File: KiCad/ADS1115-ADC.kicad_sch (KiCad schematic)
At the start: 19 parts, among them J1 Conn_01x05_Pin, U1 LM334M, U2 LM334M, U3 ADS1115IDGS

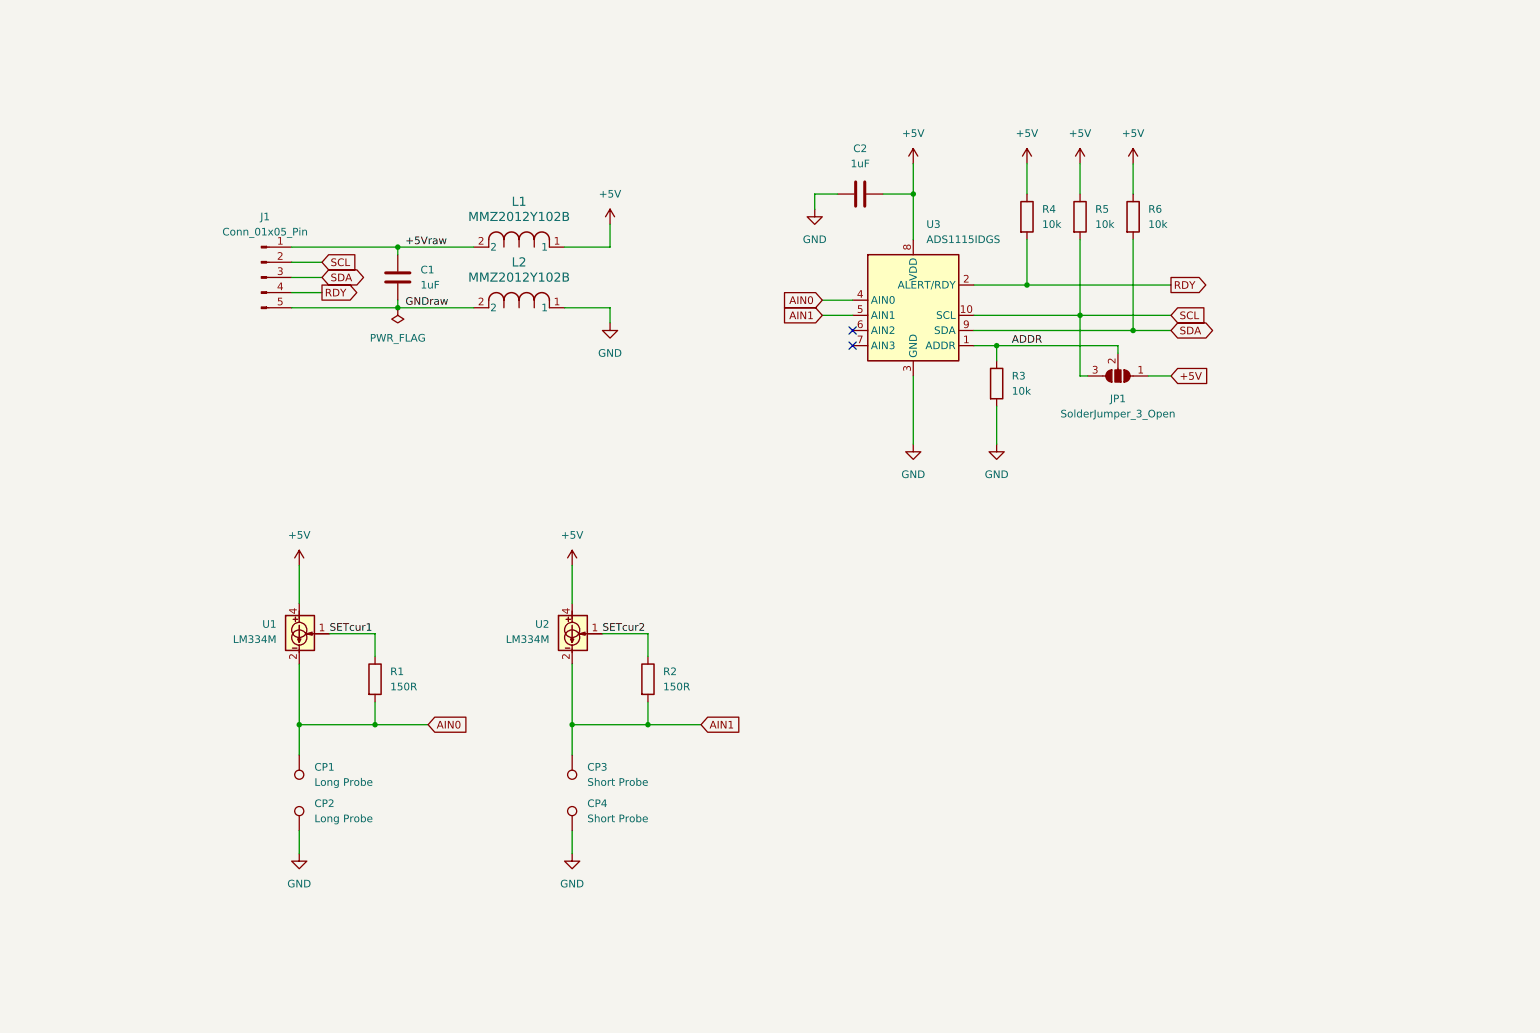
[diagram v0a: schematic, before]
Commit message: Add level shifters
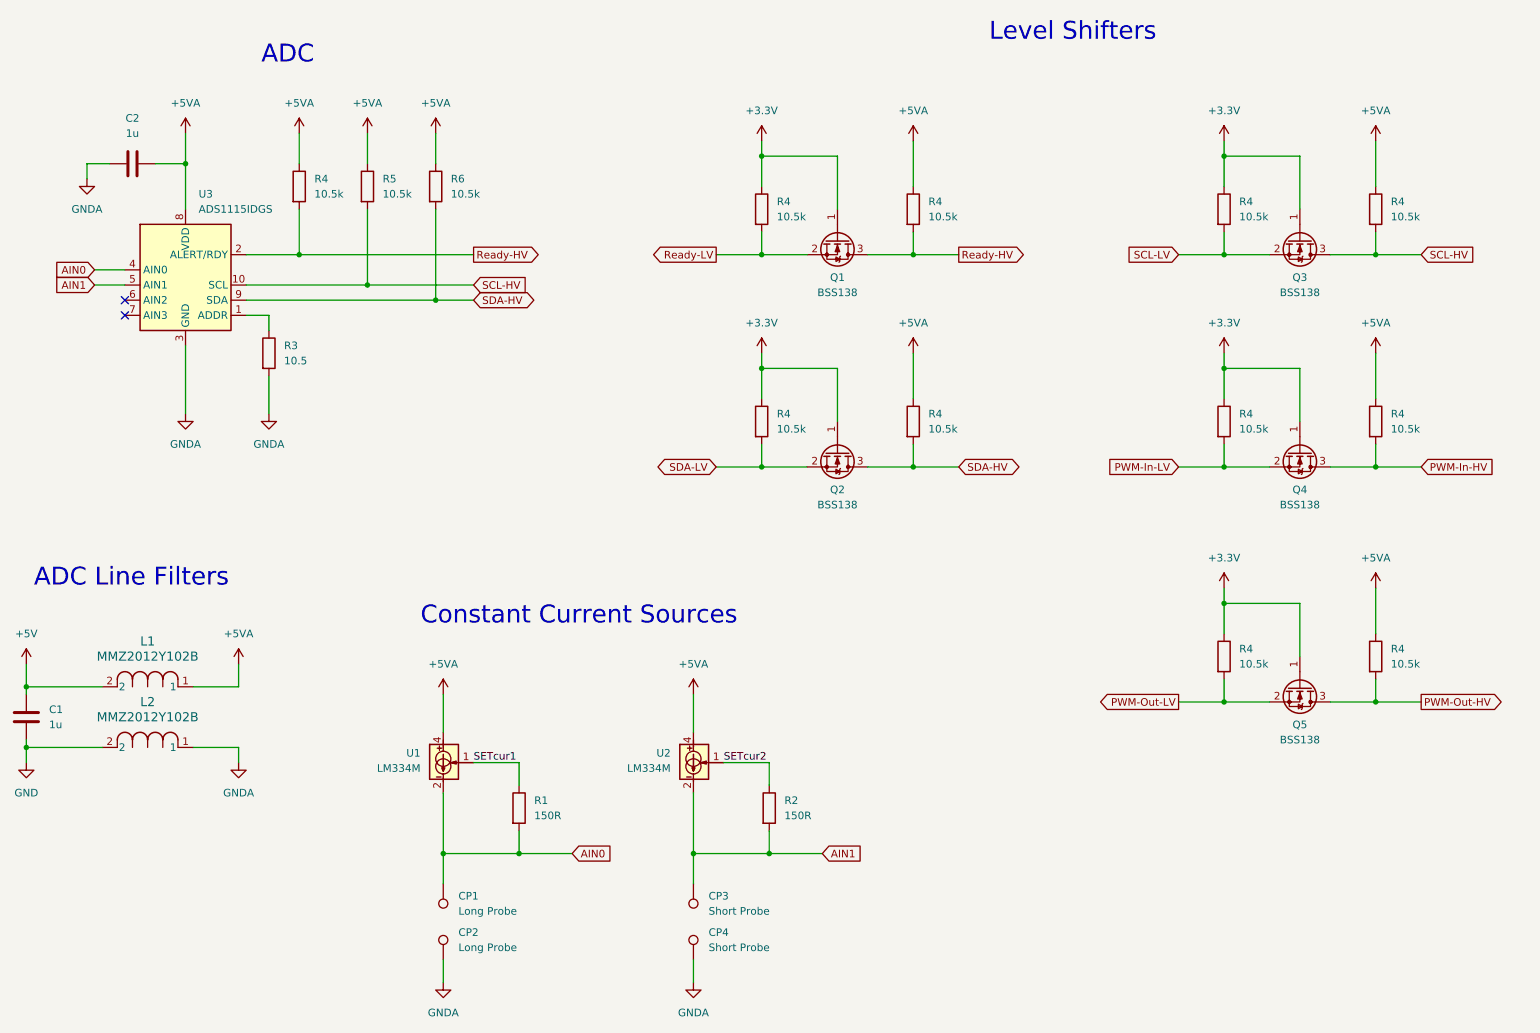
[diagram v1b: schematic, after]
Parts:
- removed J1: Conn_01x05_Pin, Connector_PinHeader_2.54mm:PinHeader_1x05_P2.54mm_Horizontal, symbol Connector:Conn_01x05_Pin
- removed JP1: SolderJumper_3_Open, Jumper:SolderJumper-3_P1.3mm_Open_RoundedPad1.0x1.5mm, symbol Jumper:SolderJumper_3_Open
- added Q1, Q2, Q3, Q4, Q5: BSS138, Package_TO_SOT_SMD:SOT-23, symbol Transistor_FET:BSS138
- added R4 (x10): 10.5k, Resistor_SMD:R_0402_1005Metric_Pad0.72x0.64mm_HandSolder, symbol Device:R
- C1, C2: value 1uF -> 1u; footprint Capacitor_SMD:C_1206_3216Metric_Pad1.33x1.80mm_HandSolder -> Capacitor_SMD:C_0402_1005Metric_Pad0.74x0.62mm_HandSolder
- R1, R2: footprint Resistor_SMD:R_1206_3216Metric_Pad1.30x1.75mm_HandSolder -> Resistor_SMD:R_0402_1005Metric_Pad0.72x0.64mm_HandSolder
- R3: value 10k -> 10.5; footprint Resistor_SMD:R_1206_3216Metric_Pad1.30x1.75mm_HandSolder -> Resistor_SMD:R_0402_1005Metric_Pad0.72x0.64mm_HandSolder
- R4, R5, R6: value 10k -> 10.5k; footprint Resistor_SMD:R_1206_3216Metric_Pad1.30x1.75mm_HandSolder -> Resistor_SMD:R_0402_1005Metric_Pad0.72x0.64mm_HandSolder
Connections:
- net +5Vraw is gone; now on net +5V: C1.1, L1.2
- net GNDraw is gone; now on net GND: C1.2, L2.2
- net +5V: no longer C2.2, L1.1, R4.1, R5.1, R6.1, U1.4, U2.4, U3.8 (VDD)
- net GND: no longer C2.1, CP2.1, CP4.1, L2.1, R3.2, U3.3 (GND)
- net ADDR: no longer names the net of R3.1, U3.1 (ADDR)
- net RDY renamed Ready-HV
- net Ready-HV: now also Q1.3 (D), R4.2
- net SCL renamed SCL-HV
- net SCL-HV: now also Q3.3 (D), R4.2
- net SDA renamed SDA-HV
- net SDA-HV: now also Q2.3 (D), R4.2
- new net +3.3V: Q1.1 (G), Q2.1 (G), Q3.1 (G), Q4.1 (G), Q5.1 (G), R4.1, R4.1, R4.1, R4.1, R4.1
- new net +5VA: C2.2, L1.1, R4.1, R4.1, R4.1, R4.1, R4.1, R4.1, R5.1, R6.1, U1.4, U2.4, U3.8 (VDD)
- new net GNDA: C2.1, CP2.1, CP4.1, L2.1, R3.2, U3.3 (GND)
- new net PWM-In-HV: Q4.3 (D), R4.2
- new net PWM-In-LV: Q4.2 (S), R4.2
- new net PWM-Out-HV: Q5.3 (D), R4.2
- new net PWM-Out-LV: Q5.2 (S), R4.2
- new net Ready-LV: Q1.2 (S), R4.2
- new net SCL-LV: Q3.2 (S), R4.2
- new net SDA-LV: Q2.2 (S), R4.2
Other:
- note added: "ADC"
- note added: "ADC Line Filters"
- note added: "Constant Current Sources"
- note added: "Level Shifters"
- moved on the sheet: C1, C2, CP1, CP2, CP3, CP4, L1, L2, R1, R2, R3, R4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

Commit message: Change resistor values
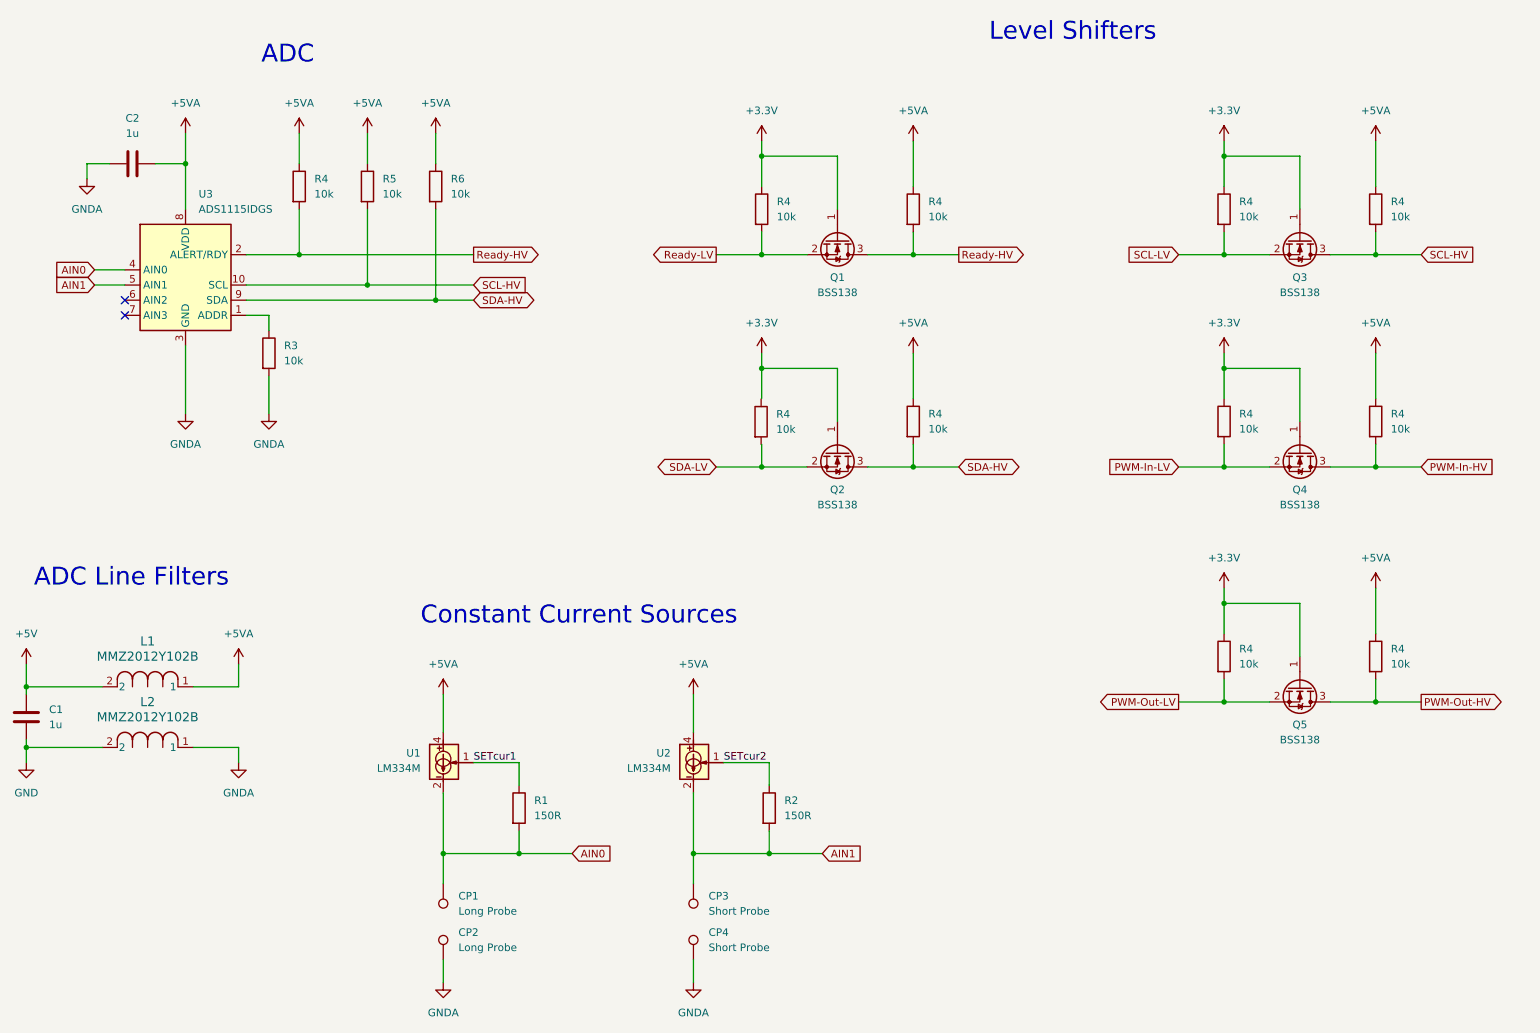
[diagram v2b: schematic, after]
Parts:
- removed R4 (x9): 10.5k, Resistor_SMD:R_0402_1005Metric_Pad0.72x0.64mm_HandSolder, symbol Device:R
- added R4 (x9): 10k, Resistor_SMD:R_0402_1005Metric_Pad0.72x0.64mm_HandSolder, symbol Device:R
- R3: value 10.5 -> 10k
- R4, R5, R6: value 10.5k -> 10k
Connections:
- net +3.3V: now also R4.1, R4.1, R4.1
- net +5VA: now also R4.1, R4.1, R4.1, R4.1, R4.1
- net PWM-In-HV: now also R4.2
- net PWM-In-LV: now also R4.2
- net PWM-Out-HV: now also R4.2
- net PWM-Out-LV: now also R4.2
- net Ready-HV: now also R4.2
- net SCL-HV: now also R4.2
- net SCL-LV: now also R4.2
- net SDA-HV: now also R4.2

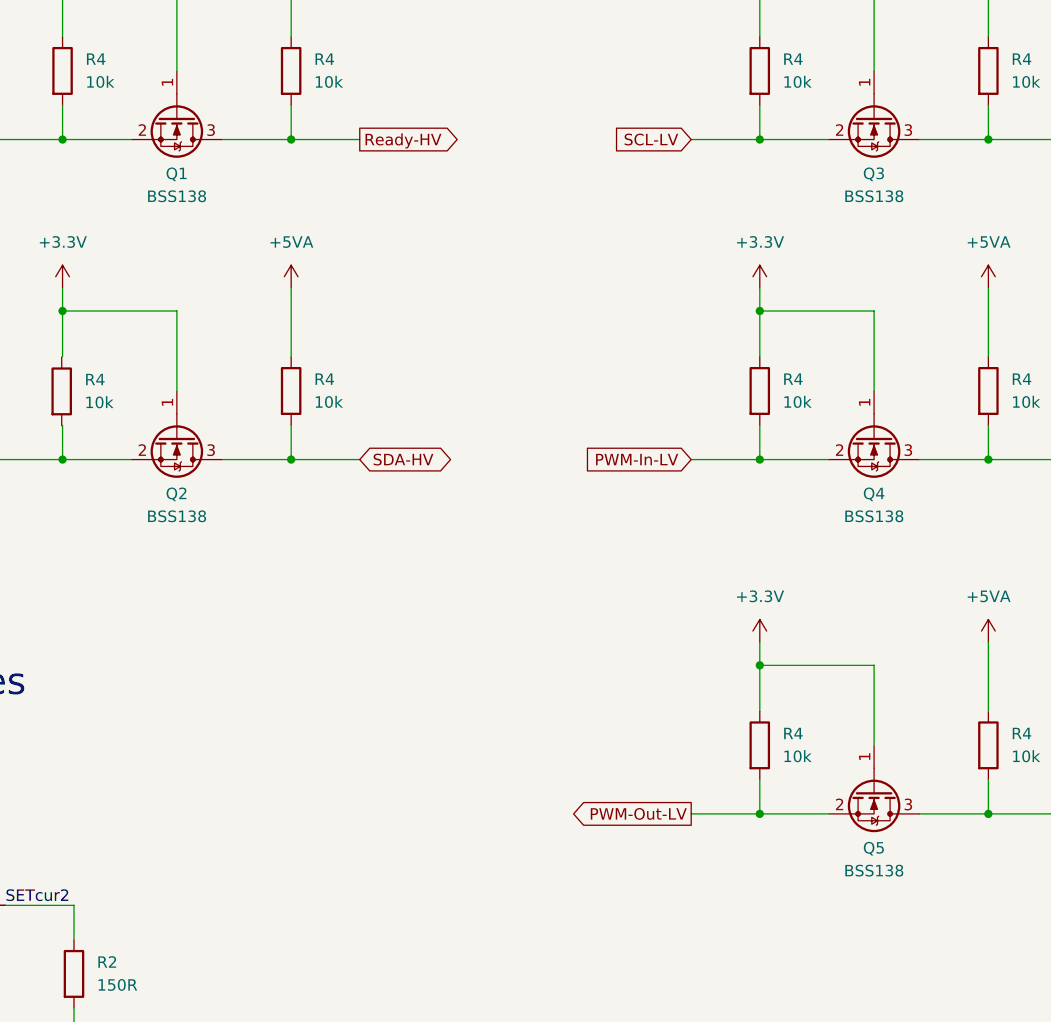
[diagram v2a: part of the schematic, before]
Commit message: Change reverse polarity protection, start the PCB design
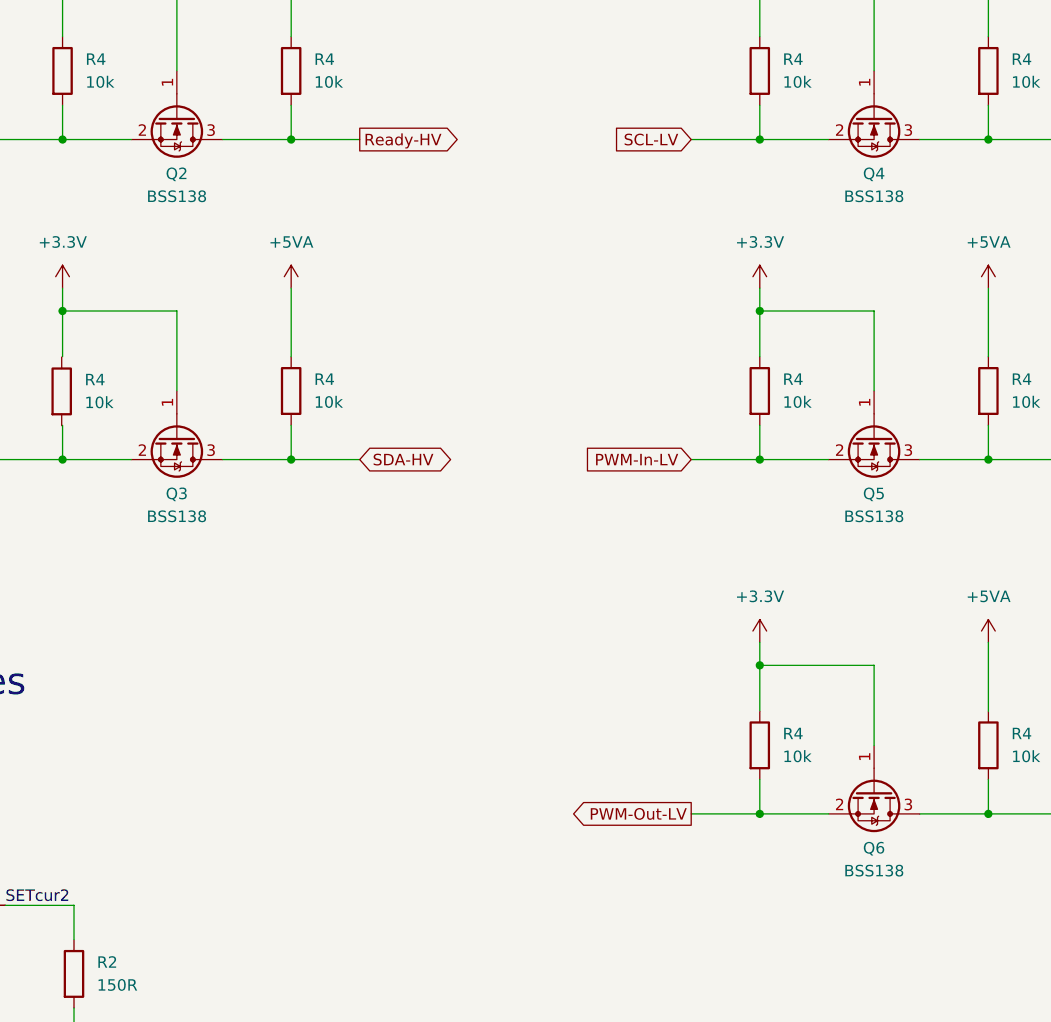
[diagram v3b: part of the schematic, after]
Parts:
- renumbered Q1 to Q2, Q2 to Q3, Q3 to Q4, Q4 to Q5, Q5 to Q6

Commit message: Use load switch, fix TC2030 pins, fix strapping pins
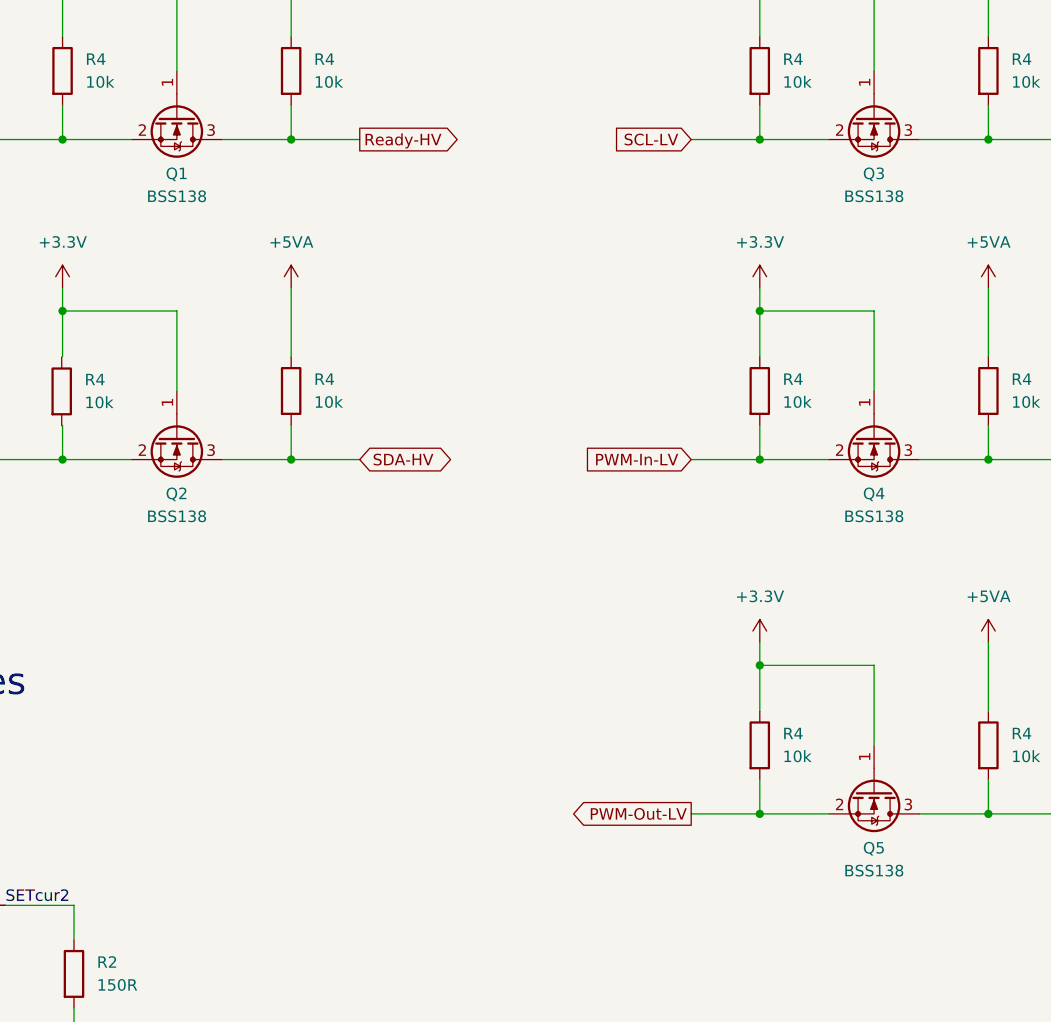
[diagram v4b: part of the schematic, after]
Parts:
- renumbered Q2 to Q1, Q3 to Q2, Q4 to Q3, Q5 to Q4, Q6 to Q5
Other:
- company: (none) -> Tamás Nagy
- title: (none) -> Hydrofoil Control

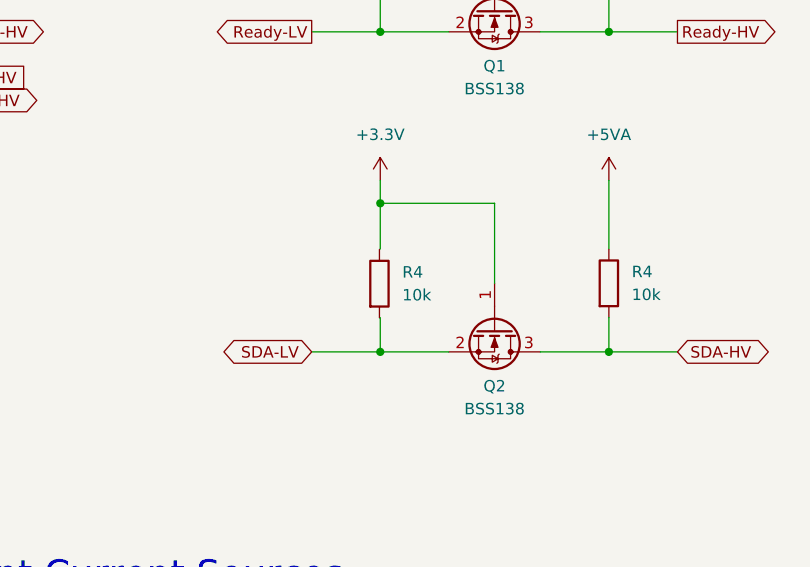
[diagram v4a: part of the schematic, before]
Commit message: Organize parts on the PCB
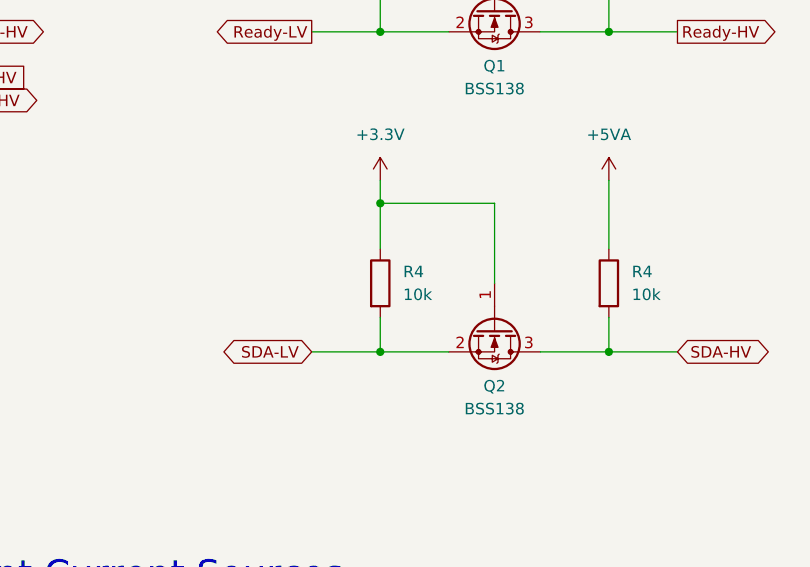
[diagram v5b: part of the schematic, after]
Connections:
- net +3.3V: now also R4.1
- net SDA-LV: now also R4.2

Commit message: Finish PCB layout, start PCB routing
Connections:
- net +5V: now also R4.1, R4.1, R4.1, R4.1, R4.1
- net +5VA: no longer R4.1, R4.1, R4.1, R4.1, R4.1
- net SETcur1 renamed Set-Curr-1
- net SETcur2 renamed Set-Curr-2
